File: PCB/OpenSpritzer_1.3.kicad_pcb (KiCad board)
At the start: 2 copper layers, 57.5 x 85 mm, 30 parts

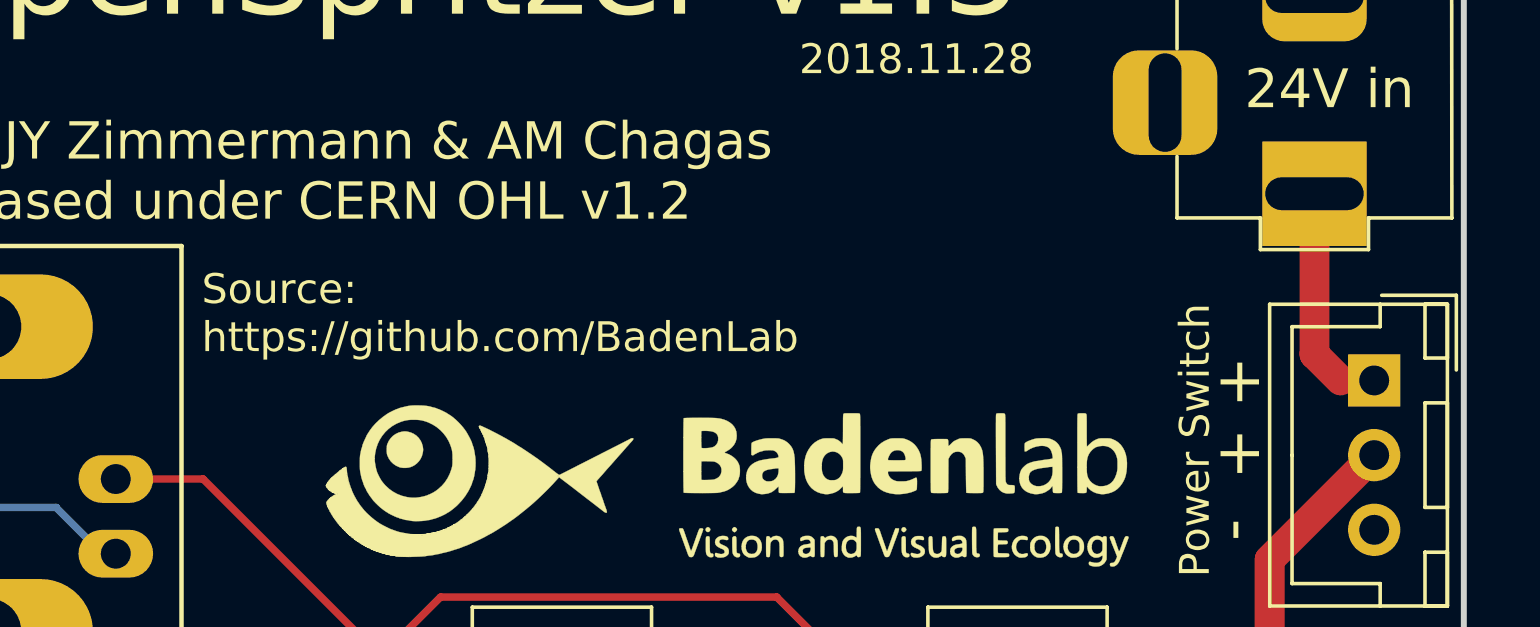
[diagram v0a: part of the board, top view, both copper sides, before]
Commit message: rename gerber to gerbers and start working on 1-click-bom.tsv
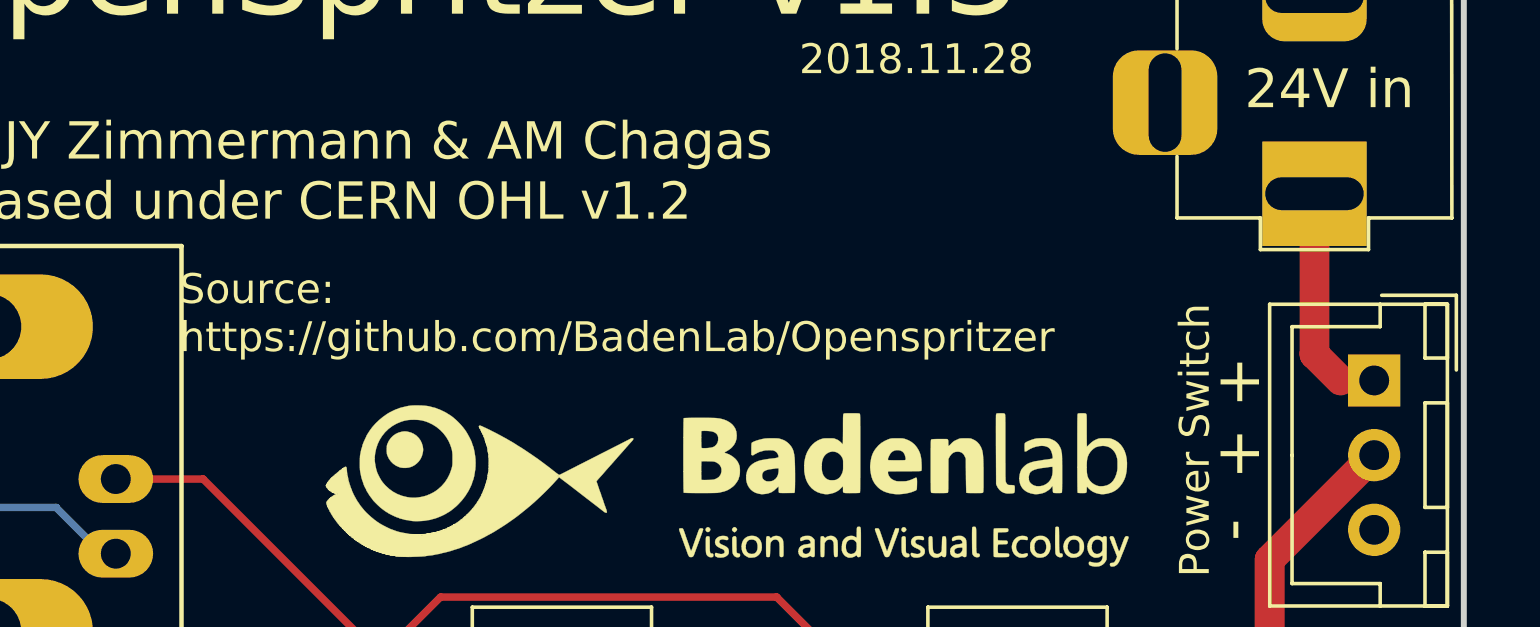
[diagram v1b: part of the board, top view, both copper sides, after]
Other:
- board text added: "Source: https://github.com/BadenLab/Openspritzer"
- board text removed: "Source: https://github.com/BadenLab"

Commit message: update PCB
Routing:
- net Net-(D4-Pad1): track 49.8 -> 13.5 mm
- net Net-(A1-Pad13): track 100.4 -> 69.2 mm
- net Net-(A1-Pad30): track 67.0 -> 38.4 mm
- net Net-(Q1-Pad2): track 26.2 -> 24.9 mm
- net Net-(J1-Pad1): track 28.2 -> 29.5 mm
- net Net-(A1-Pad5): track 12.4 -> 11.7 mm
- net Net-(D2-Pad1): track 33.9 -> 33.3 mm
- net Net-(A1-Pad27): track 97.8 -> 97.3 mm
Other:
- net class 24V removed
- net class Default removed

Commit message: update footprints
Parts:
- removed the ? at (142.8, 143.5)
- removed the ? at (154.0, 93.5)
- removed the ? at (130.2, 146.1)
- removed the ? at (130.0, 134.9)
- removed the ? at (154.0, 122.5)
- removed the ? at (100.0, 65.0)
- removed the ? at (118.0, 122.5)
- removed the ? at (118.0, 93.5)
- removed the ? at (133.0, 85.5)
- removed the ? at (100.0, 150.0)
- removed the ? at (153.3, 115.9)
- removed the ? at (152.5, 61.0)
- added C1: C_Polarized, Capacitor_THT:CP_Radial_D8.0mm_P3.50mm, F.Cu at (209.0, 111.8)
- added C2: C_Polarized, Capacitor_THT:CP_Radial_D6.3mm_P2.50mm, F.Cu at (227.8, 111.8)
- added C3: 100nF, Capacitor_THT:C_Disc_D7.5mm_W4.4mm_P5.00mm, F.Cu at (188.6, 123.0)
- added D3: D_Schottky, Diode_THT:D_DO-27_P15.24mm_Horizontal, F.Cu at (207.8, 103.5)
- added D5: LED, Connector_JST:JST_XH_B2B-XH-A_1x02_P2.50mm_Vertical, F.Cu at (204.5, 119.9)
- added J2: Barrel_Jack, Connector_JST:JST_XH_B2B-XH-A_1x02_P2.50mm_Vertical, F.Cu at (228.4, 103.5)
- added J5: on/off switch, Connector_JST:JST_XH_B2B-XH-A_1x02_P2.50mm_Vertical, F.Cu at (219.0, 110.3)
- added J6: SSD1306_screen, Connector_JST:JST_XH_B4B-XH-A_1x04_P2.50mm_Vertical, F.Cu at (190.1, 115.6)
- added R7: 1k, Resistor_THT:R_Axial_DIN0414_L11.9mm_D4.5mm_P15.24mm_Horizontal, F.Cu at (188.6, 103.1)
- added RV1: 1k, Resistor_THT:R_Axial_DIN0414_L11.9mm_D4.5mm_P15.24mm_Horizontal, F.Cu at (188.6, 109.2)
- A1: renamed from ?; value Arduino Nano v3.0 -> Arduino_Nano_v3.x; footprint Modules:Arduino_Nano_WithMountingHoles -> Module:Arduino_Nano
- D4: renamed from ?; footprint Diodes_THT:D_DO-201AD_P12.70mm_Horizontal -> Diode_THT:D_DO-201AD_P15.24mm_Horizontal
- J1: renamed from ?; value Foot Pedal -> from Foot Pedal; footprint Maxime:BNC_Socket_TYCO-AMP_LargePads -> Connector_Coaxial:BNC_Amphenol_B6252HB-NPP3G-50_Horizontal
- J3: renamed from ?; value Solenoid -> to Solenoid; footprint Maxime:JST_XH_B02B-XH-A_02x2.50mm_Straight -> Connector_JST:JST_XH_B2B-XH-A_1x02_P2.50mm_Vertical
- J4: renamed from ?; value TTL Pulse Generator -> from TTL pulse generator; footprint Maxime:BNC_Socket_TYCO-AMP_LargePads -> Connector_Coaxial:BNC_Amphenol_B6252HB-NPP3G-50_Horizontal
- L1: renamed from ?; value 33μH -> 33 uH
- R1, R2, R3: renamed from ?; value 220 Ω -> 220; footprint Maxime:R_Axial_DIN0309_L9.0mm_D3.2mm_P15.24mm_Horizontal -> Resistor_THT:R_Axial_DIN0414_L11.9mm_D4.5mm_P15.24mm_Horizontal
- R4, R5, R6: renamed from ?; value 1 kΩ -> 1k; footprint Maxime:R_Axial_DIN0309_L9.0mm_D3.2mm_P15.24mm_Horizontal -> Resistor_THT:R_Axial_DIN0414_L11.9mm_D4.5mm_P15.24mm_Horizontal
- SW1: renamed from ?; value DPDT switch -> SW_DPDT_x2; footprint Maxime:maxi_DPDT_Angled -> Button_Switch_THT:SW_Push_2P2T_Vertical_E-Switch_800UDP8P1A1M6
- moved SW1 10.4 mm to (122.5, 139.6), turned to -90 degrees
- moved J4 5.05 mm to (112.3, 129.9)
- gave numbers to parts that had none: 2
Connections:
- net Net-(A1-Pad13) renamed d10
- net Net-(A1-Pad27) renamed +5V
- net Net-(A1-Pad30) renamed +12V
- net Net-(A1-Pad8) renamed d5
- A1 pad 1: Net-(A1-Pad1) -> unconnected-(A1-Pad1)
- A1 pad 10: Net-(A1-Pad10) -> unconnected-(A1-Pad10)
- A1 pad 11: Net-(A1-Pad11) -> unconnected-(A1-Pad11)
- A1 pad 12: Net-(A1-Pad12) -> unconnected-(A1-Pad12)
- A1 pad 14: Net-(A1-Pad14) -> unconnected-(A1-Pad14)
- A1 pad 15: Net-(A1-Pad15) -> unconnected-(A1-Pad15)
- A1 pad 16: Net-(A1-Pad16) -> unconnected-(A1-Pad16)
- A1 pad 17: Net-(A1-Pad17) -> unconnected-(A1-Pad17)
- A1 pad 18: Net-(A1-Pad18) -> unconnected-(A1-Pad18)
- A1 pad 2: Net-(A1-Pad2) -> unconnected-(A1-Pad2)
- A1 pad 20: Net-(A1-Pad20) -> unconnected-(A1-Pad20)
- A1 pad 21: Net-(A1-Pad21) -> unconnected-(A1-Pad21)
- A1 pad 22: Net-(A1-Pad22) -> unconnected-(A1-Pad22)
- A1 pad 23: Net-(A1-Pad23) -> SDA
- A1 pad 24: Net-(A1-Pad24) -> SCL
- A1 pad 25: Net-(A1-Pad25) -> unconnected-(A1-Pad25)
- A1 pad 26: Net-(A1-Pad26) -> unconnected-(A1-Pad26)
- A1 pad 28: Net-(A1-Pad28) -> unconnected-(A1-Pad28)
- A1 pad 29: GNDREF -> GND
- A1 pad 3: Net-(A1-Pad3) -> unconnected-(A1-Pad3)
- A1 pad 4: GNDREF -> GND
- A1 pad 6: Net-(A1-Pad6) -> unconnected-(A1-Pad6)
- A1 pad 7: Net-(A1-Pad7) -> unconnected-(A1-Pad7)
- A1 pad 9: Net-(A1-Pad9) -> unconnected-(A1-Pad9)
- D4 pad 2: GNDREF -> GND
- J3 pad 1: Net-(C1-Pad1) -> +24V
- J4 pad 2: GNDREF -> GND
- R5 pad 2: GNDREF -> GND
- R6 pad 1: GNDREF -> GND
- U1 pad 1: Net-(C1-Pad1) -> +24V
- U1 pad 3: GNDREF -> GND
- U1 pad 5: GNDREF -> GND
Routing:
- net Net-(C1-Pad1): track 126.4 -> 7.74 mm
- net GND: track 0.00 -> 95.5 mm
- net d10: track 69.2 -> 37.0 mm
- net Net-(A1-Pad13): track 0.00 -> 32.2 mm
- net +24V: track 0.00 -> 23.5 mm
- added copper zone on B.Cu, net GND
- removed copper zone on B.Cu, net GNDREF

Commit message: update new board
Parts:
- removed ?: LED, Maxime:JST_XH_B02B-XH-A_02x2.50mm_Straight
- removed ?: Power Switch, Maxime:JST_XH_B03B-XH-A_03x2.50mm_Straight
- removed J5: on/off switch, Connector_JST:JST_XH_B2B-XH-A_1x02_P2.50mm_Vertical
- removed NPN: , Package_TO_SOT_THT:TO-92L_Inline_Wide
- added D1: LED, LED_THT:LED_D5.0mm_Horizontal_O1.27mm_Z15.0mm, F.Cu at (102.0, 106.4)
- added H1: MountingHole, MountingHole:MountingHole_3.2mm_M3_DIN965, F.Cu at (114.0, 80.0)
- added H2: MountingHole, MountingHole:MountingHole_3.2mm_M3_DIN965, F.Cu at (150.0, 93.0)
- added H3: MountingHole, MountingHole:MountingHole_3.2mm_M3_DIN965, F.Cu at (150.0, 162.9)
- added H4: MountingHole, MountingHole:MountingHole_3.2mm_M3_DIN965, F.Cu at (115.0, 162.9)
- added Q1: Q_NPN_Darlington_EBC, Package_TO_SOT_THT:TO-92L_Wide, F.Cu at (137.2, 82.3)
- added SW2: SW_DPDT_x2, Button_Switch_THT:SW_Push_2P2T_Vertical_E-Switch_800UDP8P1A1M6, F.Cu at (108.9, 85.7)
- C1: value C_Polarized -> 680µF
- C2: value C_Polarized -> 220µF
- D5: footprint Connector_JST:JST_XH_B2B-XH-A_1x02_P2.50mm_Vertical -> LED_THT:LED_D5.0mm_Horizontal_O1.27mm_Z15.0mm
- J2: value Barrel_Jack -> barrel_jack; footprint Connector_JST:JST_XH_B2B-XH-A_1x02_P2.50mm_Vertical -> Connector_BarrelJack:BarrelJack_GCT_DCJ200-10-A_Horizontal
- RV1: footprint Resistor_THT:R_Axial_DIN0414_L11.9mm_D4.5mm_P15.24mm_Horizontal -> Connector_JST:JST_XH_B3B-XH-A_1x03_P2.50mm_Vertical
- U1: footprint TO_SOT_Packages_THT:TO-220-5_Vertical_StaggeredType1 -> Package_TO_SOT_THT:TO-220-5_P3.4x3.7mm_StaggerOdd_Lead3.8mm_Vertical
- moved D5 104.6 mm to (102.0, 99.4), turned to -90 degrees
- moved C2 94.6 mm to (138.6, 143.4), turned to -90 degrees
- moved J2 85.8 mm to (145.1, 83.4), turned to 90 degrees
- moved D3 82.3 mm to (125.8, 96.6), turned to 90 degrees
- moved R7 82.2 mm to (106.4, 101.7)
- moved J1 72.2 mm to (108.5, 157.2)
- moved RV1 69.9 mm to (127.2, 142.8), turned to 180 degrees
- moved R5 68.9 mm to (120.4, 157.9)
- moved J6 66.1 mm to (127.0, 135.3), turned to 180 degrees
- moved C1 64.2 mm to (145.1, 105.2)
- moved R3 61.0 mm to (120.4, 151.9)
- moved C3 55.6 mm to (134.1, 133.9)
- moved J3 52.6 mm to (136.1, 92.5), turned to 180 degrees
- moved R2 50.0 mm to (106.4, 107.7), turned to 0 degrees
- moved SW1 46.3 mm to (109.1, 95.2), turned to 180 degrees
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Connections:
- C1 pad 1: +24V -> to_buck_conv
- D3 pad 1: +24V -> to_buck_conv
- D5 pad 2: +24V -> to_buck_conv
- J1 pad 1: Net-(J1-Pad1) -> +5V
- J1 pad 2: +5V -> Net-(J1-Pad2)
- J2 pad 1: Net-(J2-Pad1) -> +24V
- J3 pad 1: +24V -> to_buck_conv
- R3 pad 1: Net-(J1-Pad1) -> Net-(J1-Pad2)
- R5 pad 1: Net-(J1-Pad1) -> Net-(J1-Pad2)
- U1 pad 1: +24V -> to_buck_conv
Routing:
- net to_buck_conv: track 0.00 -> 121.5 mm
- net GND: track 95.5 -> 0.00 mm
- net d5: track 93.5 -> 33.7 mm
- net Net-(D2-Pad2): track 59.5 -> 6.36 mm, vias 1 -> 0
- net +5V: track 97.3 -> 47.5 mm
- net Net-(J4-Pad1): track 13.5 -> 60.0 mm
- net Net-(A1-Pad5): track 11.7 -> 52.7 mm
- net Net-(D3-Pad2): track 58.3 -> 17.5 mm
- net Net-(A1-Pad13): track 32.2 -> 0.00 mm
- net Net-(J1-Pad1): track 29.5 -> 0.00 mm
- net Net-(A1-Pad19): track 35.5 -> 11.9 mm, vias 1 -> 0
- net Net-(J1-Pad2): track 0.00 -> 20.6 mm
- net Net-(U1-Pad2): track 13.5 -> 29.9 mm, vias 2 -> 0
- net +24V: track 23.5 -> 39.2 mm
- net Net-(Q1-Pad2): track 24.9 -> 34.8 mm
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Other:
- board size 57.5 x 85 mm -> 58 x 91 mm
- board text added: "OpenSpritzer v1.4"
- board text removed: "2018.11.28"
- board text removed: "Base"
- board text removed: "Collector"
- board text removed: "Emitter"
- board text removed: "OpenSpritzer v1.3"
